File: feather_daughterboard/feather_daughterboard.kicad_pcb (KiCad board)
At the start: 2 copper layers, 80 x 11 mm, 19 parts, among them J1 61900619521

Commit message: finished daughter board
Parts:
- added G***: LOGO, Custom footprints:Logo, B.Cu at (117.7, 86.5)
- moved J1 0.96 mm to (172.1, 87.8)
- moved H1 0.85 mm to (181.8, 82.2)
- moved R2_4 0.06 mm to (112.8, 88.0)
- moved R2_2 0.05 mm to (140.8, 88.0)
- turned R2_1 to 180 degrees
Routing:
- net /Buttons/VCC: track 0.00 -> 68.2 mm
- net /Buttons/Button_4: track 2.50 -> 60.1 mm
- net /Buttons/Button_3: track 2.25 -> 42.9 mm
- net /Buttons/Button_2: track 2.30 -> 26.7 mm
- net /Buttons/Button_1: track 2.25 -> 9.10 mm, vias 0 -> 1
- net /Buttons/GND: vias 0 -> 11
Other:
- board text added: "LPRD_Feather_DaughterBoard_V1"

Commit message: finished mainboard design, need to do the routing
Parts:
- moved H2 0.10 mm to (108.5, 84.5)
- turned G*** to 0 degrees
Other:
- board size 80 x 11 mm -> 79.7 x 11 mm

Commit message: finished the mainboard, added bom files
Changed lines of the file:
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@@
 	(generator_version "8.0")
 	(general
-		(thickness 1.6)
+		(thickness 1.579)
 		(legacy_teardrops no)
 	)
@@
 	)
 	(setup
+		(stackup
+			(layer "F.SilkS"
+				(type "Top Silk Screen")
+				(color "White")
+				(material "Peters SD2692")
+			)
+			(layer "F.Paste"
+				(type "Top Solder Paste")
+			)
+			(layer "F.Mask"
+				(type "Top Solder Mask")
+				(color "Green")
+				(thickness 0.025)
+				(material "Elpemer AS 2467 SM-DG")
+				(epsilon_r 3.7)
+				(loss_tangent 0)
+			)
+			(layer "F.Cu"
+				(type "copper")
+				(thickness 0.035)
+			)
+			(layer "dielectric 1"
+				(type "core")
+				(color "FR4 natural")
+				(thickness 1.459)
+				(material "FR4")
+				(epsilon_r 4.5)
+				(loss_tangent 0.02)
+			)
+			(layer "B.Cu"
+				(type "copper")
+				(thickness 0.035)
+			)
+			(layer "B.Mask"
+				(type "Bottom Solder Mask")
+				(color "Green")
+				(thickness 0.025)
+				(material "Elpemer AS 2467 SM-DG")
+				(epsilon_r 3.7)
+				(loss_tangent 0)
+			)
+			(layer "B.Paste"
+				(type "Bottom Solder Paste")
+			)
+			(layer "B.SilkS"
+				(type "Bottom Silk Screen")
+				(color "White")
+				(material "Peters SD2692")
+			)
+			(copper_finish "ENIG")
+			(dielectric_constraints no)
+		)
 		(pad_to_mask_clearance 0)
 		(allow_soldermask_bridges_in_footprints no)
@@
 		(width 0.2)
 		(layer "F.Cu")
-		(net 3)
-	)
-	(segment
-		(start 164.64055 85.5533)
-		(end 164.66555 85.5783)
-		(width 0.2)
-		(layer "F.Cu")

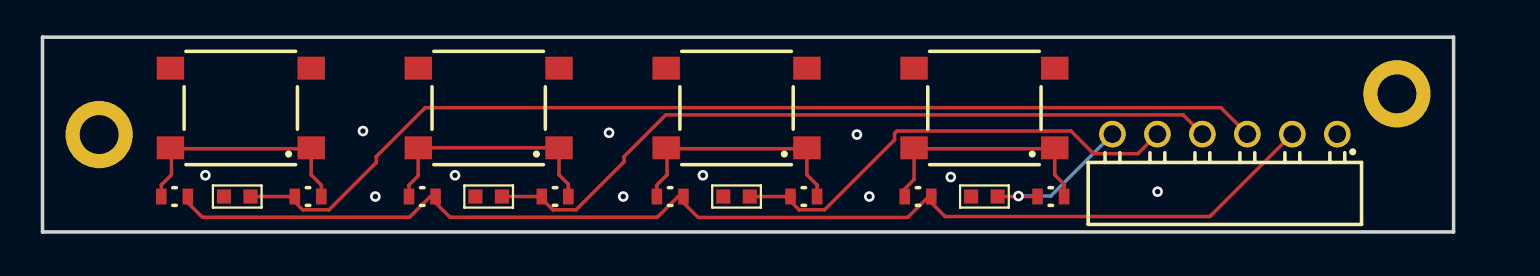
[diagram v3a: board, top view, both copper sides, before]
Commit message: changed the connector on the daughter board
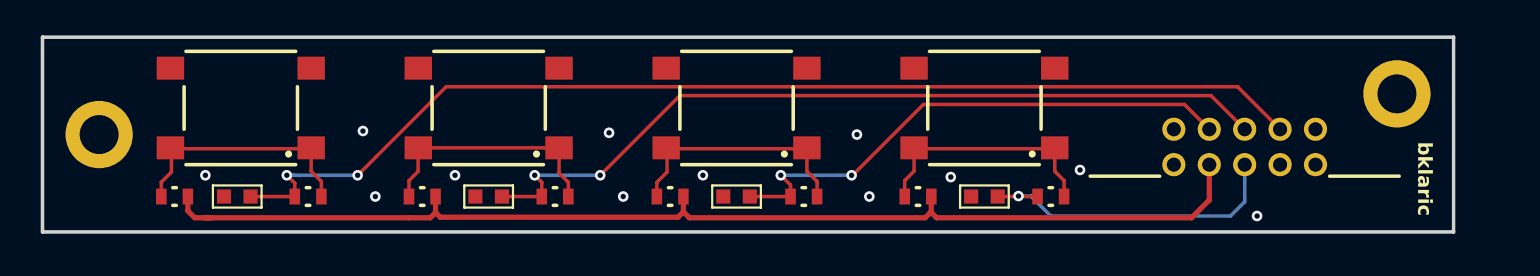
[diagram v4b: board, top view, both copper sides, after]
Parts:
- J1: value 61900619521 -> 6250XX21721_62501021721; footprint Custom footprints:61900619521 -> Custom footprints:62501021721
- moved J1 2.23 mm to (173.2, 89.8)
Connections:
- J1 pad 1: /Buttons/GND -> unconnected-(J1-Pad1)
- J1 pad 2: /Buttons/VCC -> unconnected-(J1-Pad2)
- J1 pad 4: /Buttons/Button_3 -> /Buttons/GND
- J1 pad 5: /Buttons/Button_2 -> /Buttons/Button_3
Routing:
- net /Buttons/Button_1: track 9.10 -> 18.0 mm
- net /Buttons/Button_3: track 42.8 -> 46.4 mm, vias 0 -> 2
- net /Buttons/Button_2: track 26.6 -> 30.2 mm, vias 0 -> 2
- net /Buttons/Button_4: track 60.1 -> 63.1 mm, vias 0 -> 2
- net /Buttons/VCC: track 68.2 -> 65.4 mm
- net /Buttons/GND: vias 11 -> 12
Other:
- board text added: "bklaric"

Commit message: finished mainboard and daughterboard
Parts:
- removed H2: MountingHole_Pad, MountingHole:MountingHole_2.2mm_M2_DIN965_Pad
- moved J1 5.11 mm to (168.8, 87.2)
- moved S1 5.00 mm to (153.5, 83.0)
- moved C1_1 4.98 mm to (153.5, 88.0)
- moved R1_1 4.98 mm to (157.3, 88.0)
- moved R2_1 4.98 mm to (149.8, 88.0)
- moved C1_2 3.50 mm to (141.0, 88.0)
- moved R1_2 3.50 mm to (144.8, 88.0)
- moved R2_2 3.50 mm to (137.2, 88.0)
- moved S2 3.50 mm to (141.0, 83.0)
- moved H1 2.32 mm to (181.5, 84.5)
- moved C1_3 2.00 mm to (128.5, 88.0)
- moved R1_3 2.00 mm to (132.2, 88.0)
- moved R2_3 2.00 mm to (124.8, 88.0)
- moved S3 2.00 mm to (128.5, 83.0)
- moved G*** 1.63 mm to (116.6, 85.3)
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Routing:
- net /Buttons/Button_4: track 63.1 -> 59.8 mm
- net /Buttons/VCC: track 65.4 -> 63.2 mm
- net /Buttons/Button_1: track 18.0 -> 19.7 mm
- net /Buttons/Button_3: track 46.4 -> 44.7 mm
- net /Buttons/GND: vias 12 -> 19
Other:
- board size 79.7 x 11 mm -> 76.5 x 11 mm

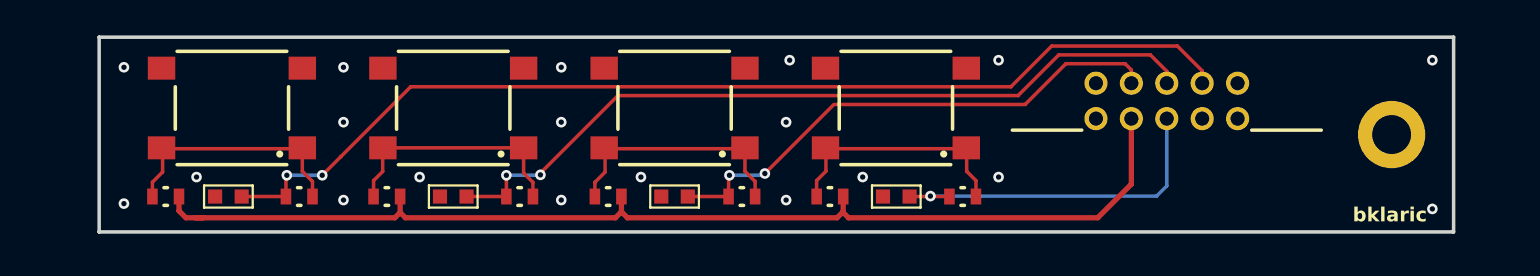
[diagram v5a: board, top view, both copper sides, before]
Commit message: added bigger logo and labeled the pins on the connectors
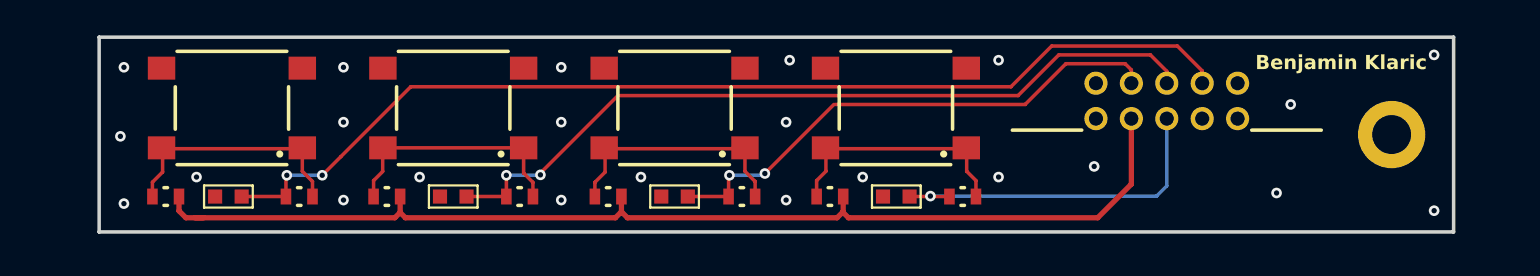
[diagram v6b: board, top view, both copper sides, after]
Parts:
- removed G***: LOGO, Custom footprints:Logo
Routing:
- net /Buttons/GND: vias 19 -> 23
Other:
- board text added: "1"
- board text added: "10"
- board text added: "2"
- board text added: "9"
- board text added: "B_1"
- board text added: "B_2"
- board text added: "B_3"
- board text added: "B_4"
- board text added: "Benjamin Klaric"
- board text added: "GND"
- board text added: "VCC"
- board text removed: "bklaric"

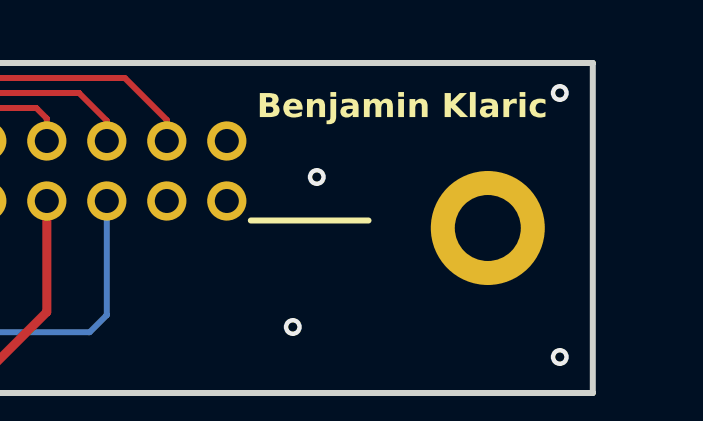
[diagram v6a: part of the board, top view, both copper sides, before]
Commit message: Small changed to daughterboard silkscreen text
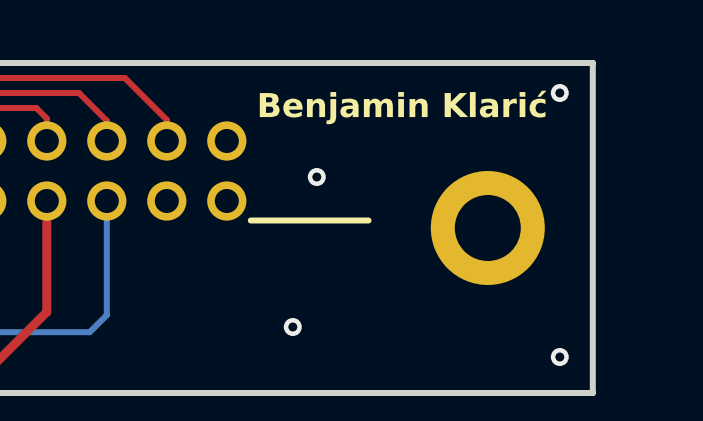
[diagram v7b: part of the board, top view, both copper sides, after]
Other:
- board text added: "Benjamin Klarić"
- board text added: "LPRD_Feather_Daughterboard_V1.1"
- board text removed: "Benjamin Klaric"
- board text removed: "LPRD_Feather_DaughterBoard_V1"
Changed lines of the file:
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@@
 		)
 	)
-	(gr_text "LPRD_Feather_DaughterBoard_V1"
-		(at 158.8 83 0)
+	(gr_text "LPRD_Feather_Daughterboard_V1.1"
+		(at 159.8 83 0)
 		(layer "B.SilkS")
 		(effects
@@
 		)
 	)
-	(gr_text "Benjamin Klaric"
+	(gr_text "Benjamin Klarić"
 		(at 173.8 80.9 0)
 		(layer "F.SilkS")

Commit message: Updated Daughterboard and added Gerber files
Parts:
- removed H1: MountingHole_Pad, MountingHole:MountingHole_2.2mm_M2_DIN965_Pad
- added H2: MountingHole_Pad, MountingHole:MountingHole_2.2mm_M2_DIN965_Pad, F.Cu at (181.5, 84.5)
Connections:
- net /Buttons/Button_1 renamed /Board/Button_1
- net /Buttons/Button_2 renamed /Board/Button_2
- net /Buttons/Button_3 renamed /Board/Button_3
- net /Buttons/Button_4 renamed /Board/Button_4
- net /Buttons/GND renamed /Board/GND
- net /Buttons/VCC renamed /Board/VCC
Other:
- board text added: "LPRD_Feather_Daughterboard_V2.1"
- board text removed: "LPRD_Feather_Daughterboard_V1.1"
